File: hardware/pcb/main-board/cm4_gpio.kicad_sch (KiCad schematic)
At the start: 14 parts, among them J402 CM4Lite SD Card, U402 RT9742SNGV

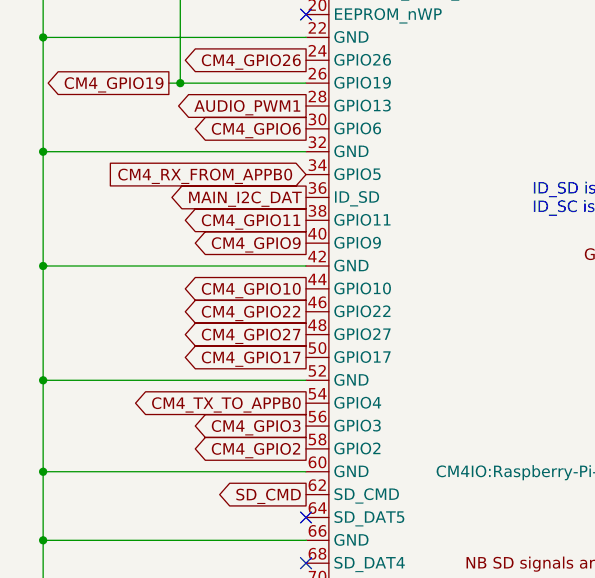
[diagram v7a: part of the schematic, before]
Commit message: rename app board picos to 1 and 2, to match the application board schematics
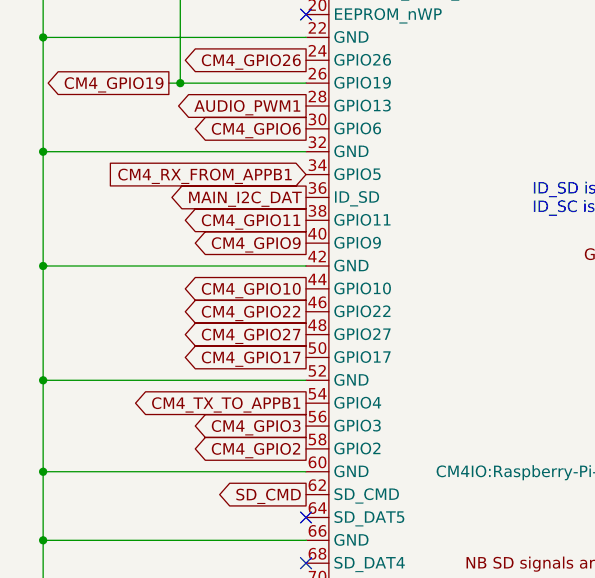
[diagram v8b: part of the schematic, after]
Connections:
- net CM4_RX_FROM_APPB0: no longer Module301.34 (GPIO5)
- net CM4_TX_TO_APPB0: no longer Module301.54 (GPIO4)
- new net CM4_RX_FROM_APPB1: Module301.34 (GPIO5)
- new net CM4_TX_TO_APPB1: Module301.54 (GPIO4)
